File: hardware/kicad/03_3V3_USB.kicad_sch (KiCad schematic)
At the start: 8 parts, among them U301 TPS2116DRLR, U302 NCV1117ST33T3G

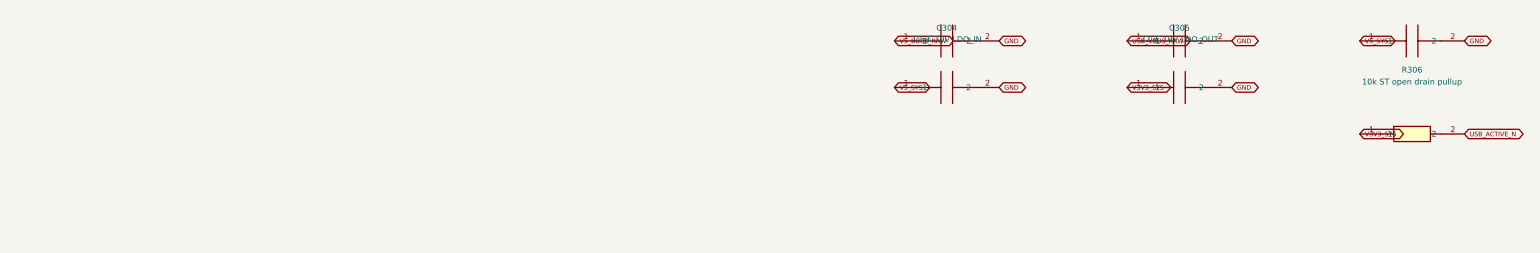
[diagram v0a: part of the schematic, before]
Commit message: fix(power): guarantee NCV1117 output capacitor series ESR using dedicated 0.10-ohm resistor
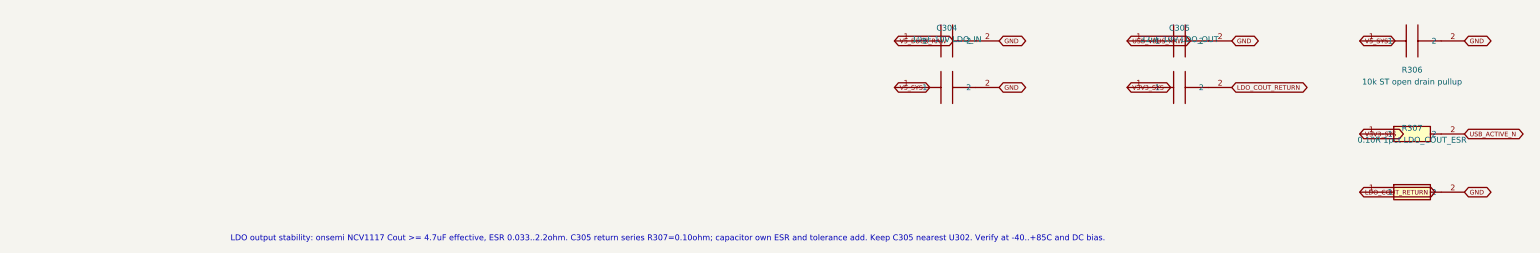
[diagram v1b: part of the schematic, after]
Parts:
- added R307: 0.10R 1pct LDO_COUT_ESR, Tripmaster:R_1206_3216, symbol Tripmaster_Sym:R
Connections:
- net GND: now also R307.2; no longer C305.2
- new net LDO_COUT_RETURN: C305.2, R307.1
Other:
- note added: "LDO output stability: onsemi NCV1117 Cout >= 4.7uF effective, ESR 0.033..2.2ohm. C305 return series R307=0.10ohm; capacitor own ESR and tolerance add. Keep C305 nearest U302. Verify at -40..+85C and DC bias."

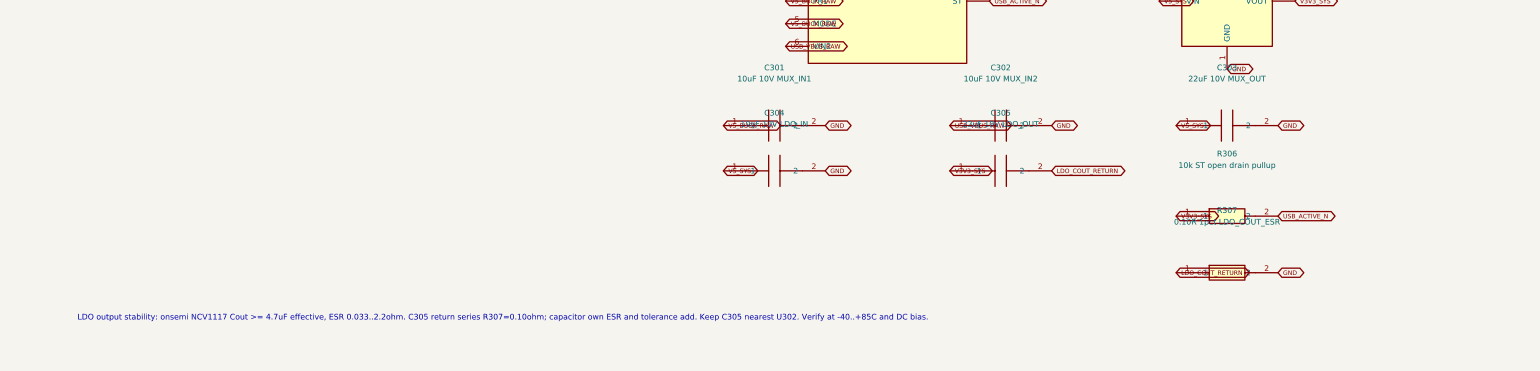
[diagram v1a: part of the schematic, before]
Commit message: hardware(power): add second post-mux 22uF capacitor for USB/vehicle transition headroom
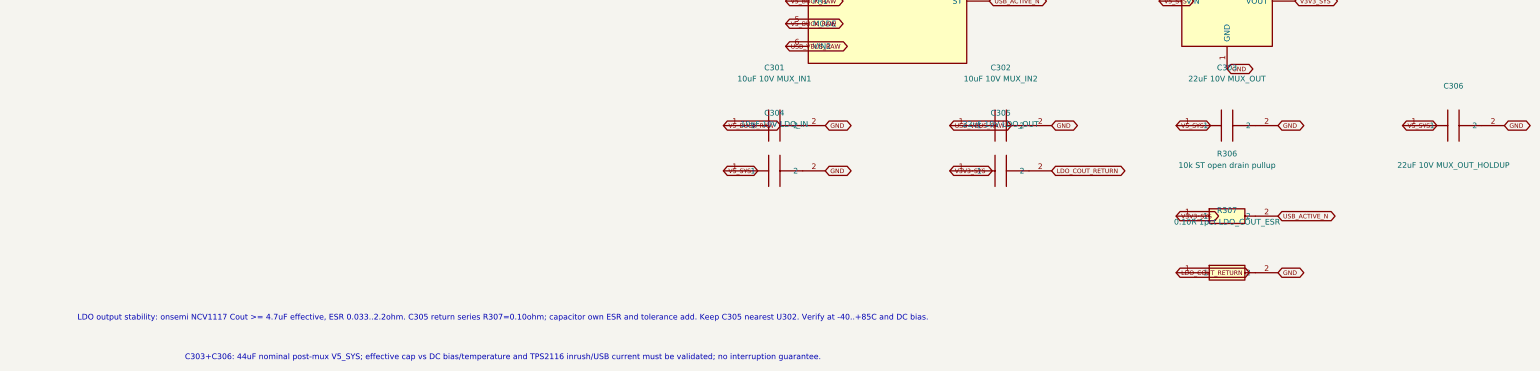
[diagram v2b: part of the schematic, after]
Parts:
- added C306: 22uF 10V MUX_OUT_HOLDUP, Tripmaster:C_1210_3225, symbol Tripmaster_Sym:C
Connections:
- net GND: now also C306.2
- net V5_SYS: now also C306.1
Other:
- note added: "C303+C306: 44uF nominal post-mux V5_SYS; effective cap vs DC bias/temperature and TPS2116 inrush/USB current must be validated; no interruption guarantee."

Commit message: fix(power): replace unsafe TPS2116 PR1=VIN1 tie with 100k/30.1k priority threshold divider
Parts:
- added R308: 100k 1% PR1_TOP, Tripmaster:R_1206_3216, symbol Tripmaster_Sym:R
- added R309: 30.1k 1% PR1_BOTTOM, Tripmaster:R_1206_3216, symbol Tripmaster_Sym:R
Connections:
- net GND: now also R309.2
- net V5_BUCK_RAW: now also R308.1; no longer U301.4 (PR1)
- new net MUX_PRI1_SENSE: R308.2, R309.1, U301.4 (PR1)
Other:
- note added: "TPS2116 priority threshold: R308=100k +/-1%, R309=30.1k +/-1% -> nominal VIN1 switch ~4.32V. VREF=0.92..1.08V guaranteed -40..105C, I_PR1 <=0.1uA. PR1 MUST NOT BE TIED DIRECTLY TO VIN1. MODE remains tied VIN1."
- note added: "U301 TPS2116 DRL8: VIN1 BUCK -> PRIORITY (PR1=R308/R309 divider, MODE=VIN1), VIN2 USB VBUS, reverse-current blocking. Voltage domain 1.6..5.5V ONLY. Device USB requires upstream 5V current budget/ESD. U302 NCV1117 3V3 requires minimum-load/ESR and thermal test."
- note removed: "U301 TPS2116 DRL8: VIN1 BUCK -> PRIORITY (PR1=VIN1, MODE=VIN1), VIN2 USB VBUS, reverse-current blocking. Voltage domain 1.6..5.5V ONLY. Device USB requires upstream 5V current budget/ESD. U302 NCV1117 3V3 requires minimum-load/ESR and thermal test."

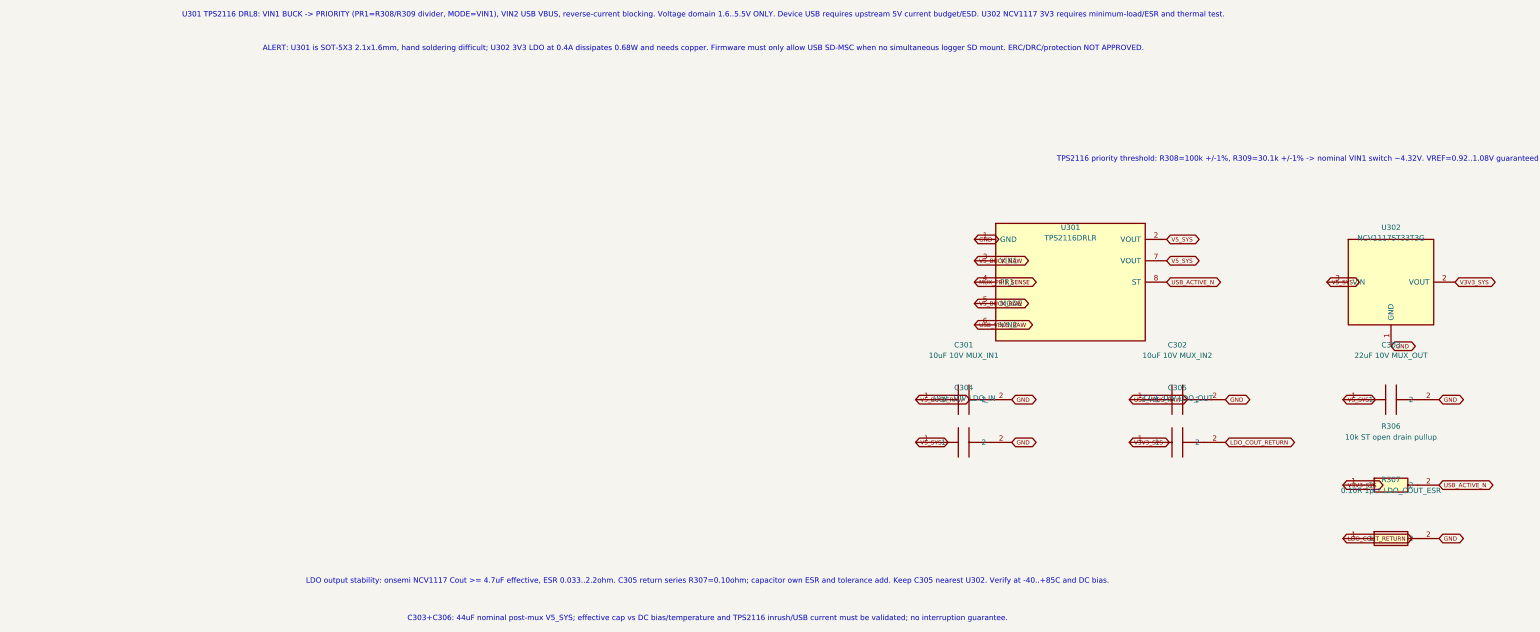
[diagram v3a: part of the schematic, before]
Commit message: hardware(power): replace high-dropout NCV1117 with MCP1826S and simplify ceramic output return
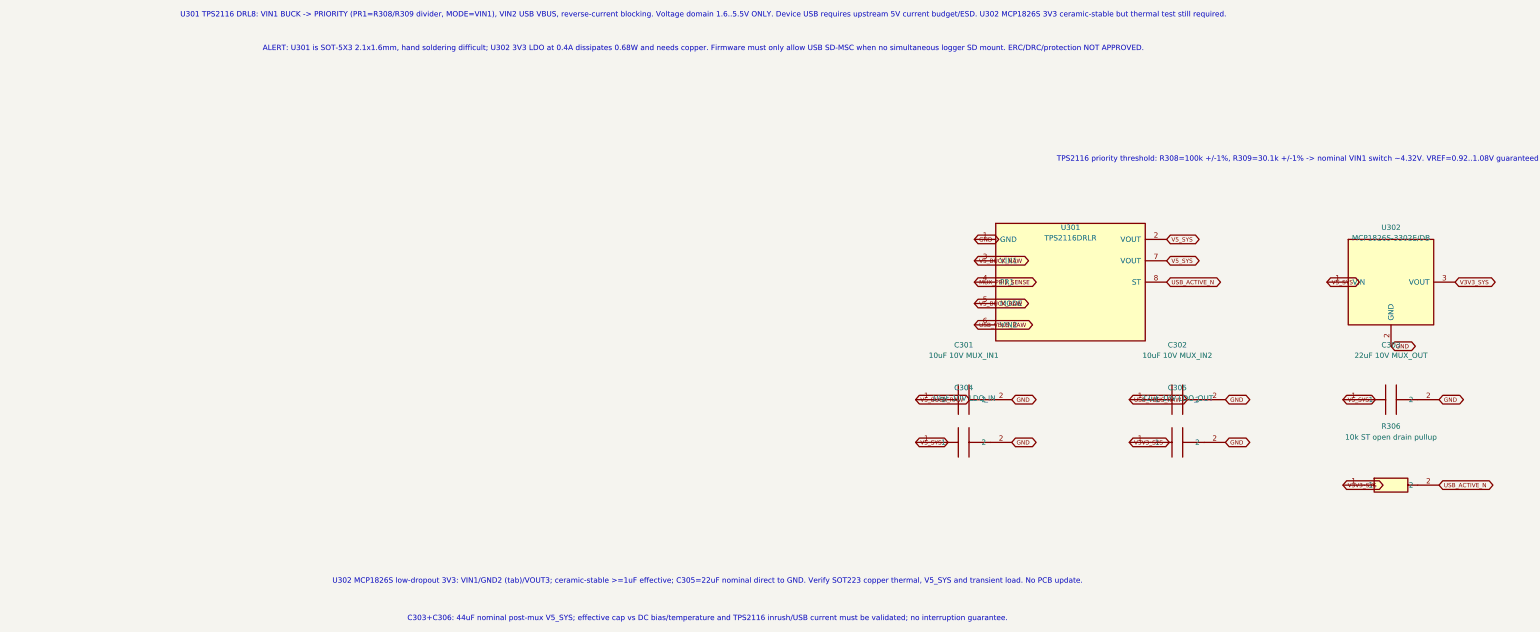
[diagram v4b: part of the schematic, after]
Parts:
- removed R307: 0.10R 1pct LDO_COUT_ESR, Tripmaster:R_1206_3216, symbol Tripmaster_Sym:R
- U302: value NCV1117ST33T3G -> MCP1826S-3302E/DB; symbol TripTracer_V1:NCV1117_3V3 -> TripTracer_V1:MCP1826S_3V3
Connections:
- net LDO_COUT_RETURN is gone; now on net GND: C305.2
- net GND: now also U302.2 (GND); no longer U302.1 (GND)
- net V3V3_SYS: now also U302.3 (VOUT); no longer U302.2 (VOUT)
- net V5_SYS: now also U302.1 (VIN); no longer U302.3 (VIN)
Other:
- note added: "U301 TPS2116 DRL8: VIN1 BUCK -> PRIORITY (PR1=R308/R309 divider, MODE=VIN1), VIN2 USB VBUS, reverse-current blocking. Voltage domain 1.6..5.5V ONLY. Device USB requires upstream 5V current budget/ESD. U302 MCP1826S 3V3 ceramic-stable but thermal test still required."
- note added: "U302 MCP1826S low-dropout 3V3: VIN1/GND2 (tab)/VOUT3; ceramic-stable >=1uF effective; C305=22uF nominal direct to GND. Verify SOT223 copper thermal, V5_SYS and transient load. No PCB update."
- note removed: "LDO output stability: onsemi NCV1117 Cout >= 4.7uF effective, ESR 0.033..2.2ohm. C305 return series R307=0.10ohm; capacitor own ESR and tolerance add. Keep C305 nearest U302. Verify at -40..+85C and DC bias."
- note removed: "U301 TPS2116 DRL8: VIN1 BUCK -> PRIORITY (PR1=R308/R309 divider, MODE=VIN1), VIN2 USB VBUS, reverse-current blocking. Voltage domain 1.6..5.5V ONLY. Device USB requires upstream 5V current budget/ESD. U302 NCV1117 3V3 requires minimum-load/ESR and thermal test."

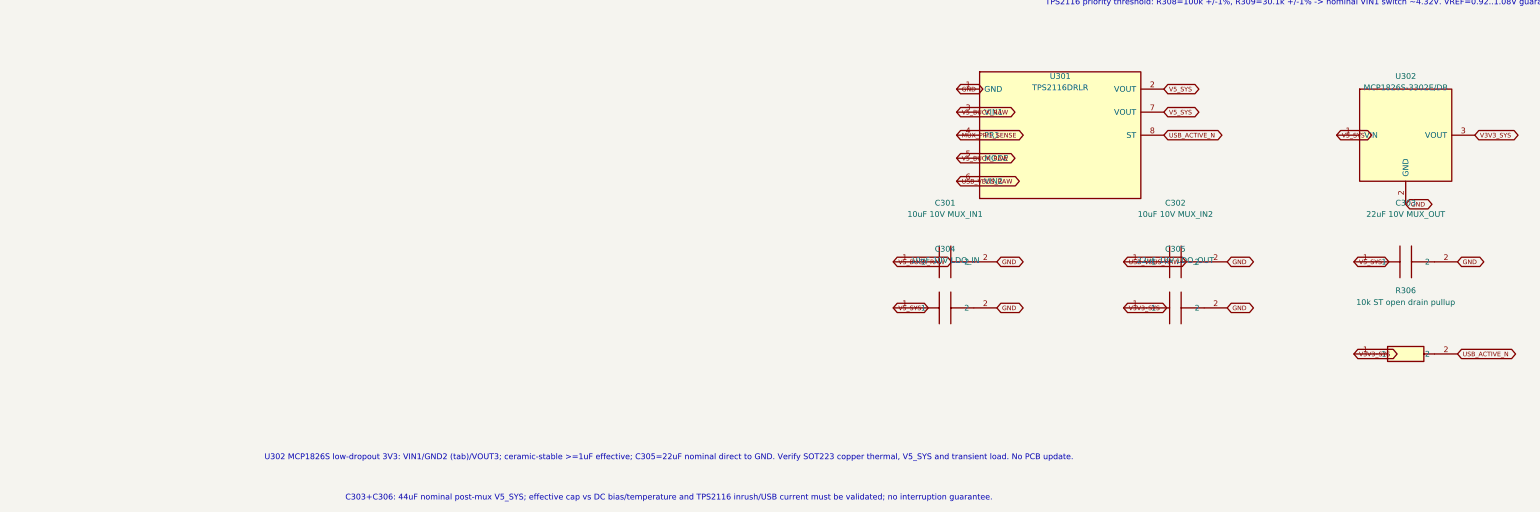
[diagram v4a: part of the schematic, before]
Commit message: hardware(power): select DDPAK MCP1826S 3V3 to improve safe hot-ambient dissipation
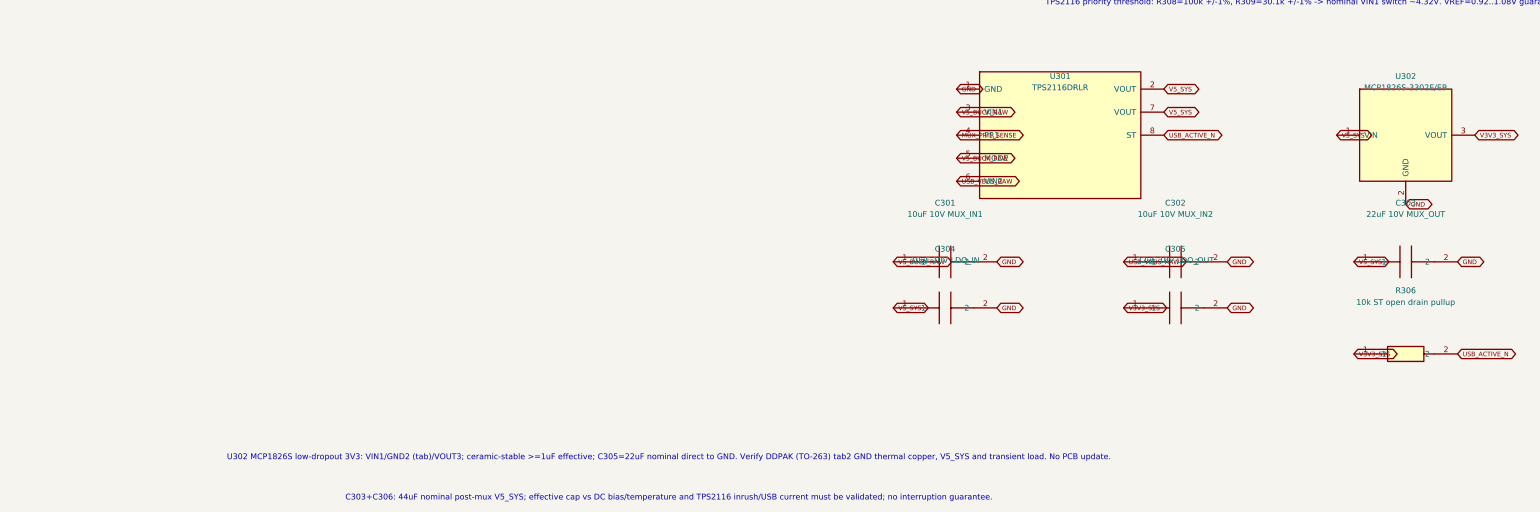
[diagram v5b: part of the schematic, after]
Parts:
- U302: value MCP1826S-3302E/DB -> MCP1826S-3302E/EB; footprint Package_TO_SOT_SMD:SOT-223-3_TabPin2 -> Package_TO_SOT_SMD:TO-263-3_TabPin2
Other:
- note added: "U302 MCP1826S low-dropout 3V3: VIN1/GND2 (tab)/VOUT3; ceramic-stable >=1uF effective; C305=22uF nominal direct to GND. Verify DDPAK (TO-263) tab2 GND thermal copper, V5_SYS and transient load. No PCB update."
- note removed: "U302 MCP1826S low-dropout 3V3: VIN1/GND2 (tab)/VOUT3; ceramic-stable >=1uF effective; C305=22uF nominal direct to GND. Verify SOT223 copper thermal, V5_SYS and transient load. No PCB update."

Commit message: fix(ERC): explicitly declare physically connected external BAT/GND and USB sources, not invented internal power
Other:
- note added: "ERC external power declarations ONLY: flags identify a real conditional external source through J901 fused BAT+/GND (01G) or USB-C J201 VBUS (03). Do not confuse ERC pass with electrical load-dump, current, fuse, or automotive safety qualification."
